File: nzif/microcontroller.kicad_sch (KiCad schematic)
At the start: 25 parts, among them U1 MCP23017_SO

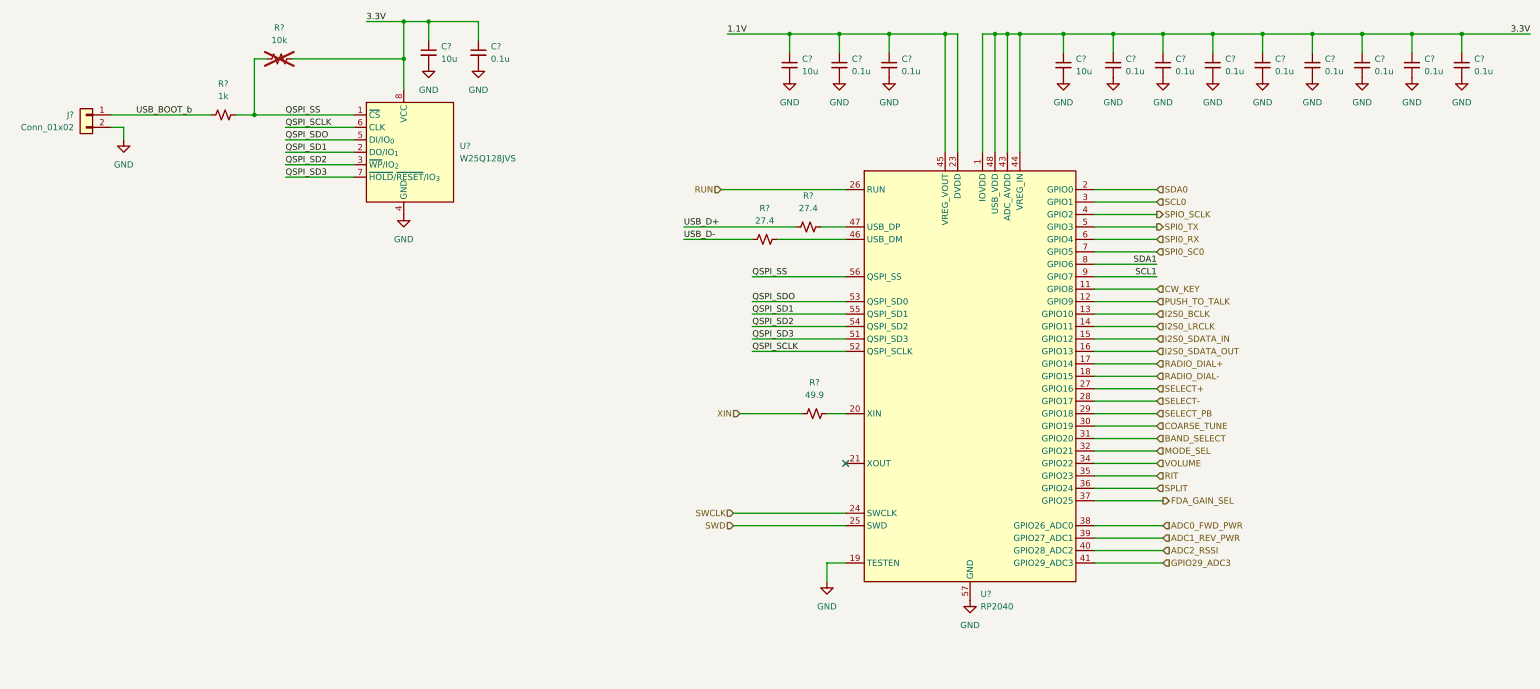
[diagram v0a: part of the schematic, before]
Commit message: Fix op amps to be correct units
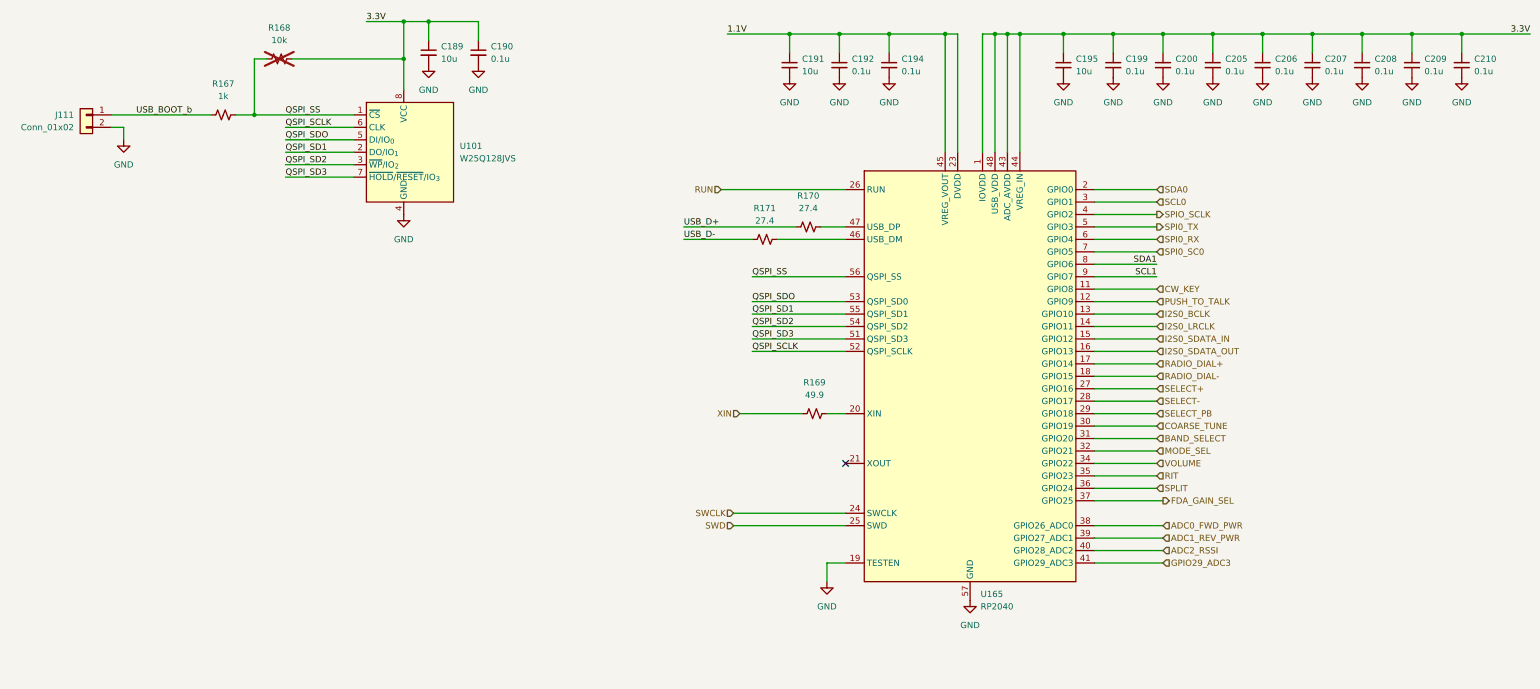
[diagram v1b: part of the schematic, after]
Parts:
- gave numbers to parts that had none: 22
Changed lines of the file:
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@@
 		(dnp no)
 		(fields_autoplaced yes)
-		(property "Reference" "C?"
+		(property "Reference" "C189"
 			(at 118.11 33.0262 0)
 			(effects
@@
 		(dnp yes)
 		(fields_autoplaced yes)
-		(property "Reference" "R?"
+		(property "Reference" "R168"
 			(at 85.09 29.21 90)
 			(effects
@@
 		(dnp no)
 		(fields_autoplaced yes)
-		(property "Reference" "R?"
+		(property "Reference" "R170"
 			(at 193.04 63.5 90)
 			(effects
@@
 		(dnp no)
 		(fields_autoplaced yes)
-		(property "Reference" "#PWR?"
+		(property "Reference" "#PWR0120"
 			(at 189.23 45.72 0)
 			(effects
@@
 		(dnp no)
 		(fields_autoplaced yes)
-		(property "Reference" "C?"
+		(property "Reference" "C194"
 			(at 212.09 35.5662 0)
 			(effects
@@
 		(dnp no)
 		(fields_autoplaced yes)
-		(property "Reference" "#PWR?"
+		(property "Reference" "#PWR0236"
 			(at 226.06 152.4 0)
 			(effects
@@
 		(dnp no)
 		(fields_autoplaced yes)
-		(property "Reference" "#PWR?"
+		(property "Reference" "#PWR0126"
 			(at 209.55 45.72 0)
 			(effects
@@
 		(dnp no)
 		(fields_autoplaced yes)
-		(property "Reference" "C?"
+		(property "Reference" "C207"
 			(at 298.45 35.5662 0)
 			(effects
@@
 		(dnp no)
 		(fields_autoplaced yes)
-		(property "Reference" "#PWR01"
+		(property "Reference" "#PWR?"
 			(at 195.58 189.23 0)
 			(effects
@@
 				)
 			)
+			(project "nzif"
+				(path "/fe42ca2f-2bb8-4d5a-9e84-807788ed632f/27cecad5-c0fc-4afc-95d0-cabdd6a56668"
+					(reference "#PWR?")
+					(unit 1)
+				)
+			)
 		)
 	)
@@
 		(dnp no)
 		(fields_autoplaced yes)
-		(property "Reference" "#PWR?"
+		(property "Reference" "#PWR0222"
 			(at 255.27 45.72 0)
 			(effects
@@
 		(dnp no)
 		(fields_autoplaced yes)
-		(property "Reference" "C?"
+		(property "Reference" "C208"
 			(at 308.61 35.5662 0)
 			(effects
@@
 		(dnp no)
 		(fields_autoplaced yes)
-		(property "Reference" "C?"
+		(property "Reference" "C190"
 			(at 128.27 33.0262 0)
 			(effects
@@
 		(dnp no)
 		(fields_autoplaced yes)
-		(property "Reference" "R?"
+		(property "Reference" "R169"
 			(at 194.31 101.6 90)
 			(effects
@@
 		(dnp no)
 		(fields_autoplaced yes)
-		(property "Reference" "#PWR?"
+		(property "Reference" "#PWR0223"
 			(at 265.43 45.72 0)
 			(effects
@@
 		(dnp no)
 		(fields_autoplaced yes)
-		(property "Reference" "R?"
+		(property "Reference" "R167"
 			(at 73.66 40.64 90)
 			(effects
@@
 		(dnp no)
 		(fields_autoplaced yes)
-		(property "Reference" "#PWR?"
+		(property "Reference" "#PWR0238"
 			(at 215.9 251.46 0)
 			(effects
@@
 		(dnp no)
 		(fields_autoplaced yes)
-		(property "Reference" "C?"
+		(property "Reference" "C210"
 			(at 328.93 35.5662 0)
 			(effects
@@
 		(dnp no)
 		(fields_autoplaced yes)
-		(property "Reference" "C?"
+		(property "Reference" "C200"
 			(at 267.97 35.5662 0)
 			(effects
@@
 		(dnp no)
 		(fields_autoplaced yes)
-		(property "Reference" "R?"
+		(property "Reference" "R171"
 			(at 184.15 66.04 90)
 			(effects
@@
 		(dnp no)
 		(fields_autoplaced yes)
-		(property "Reference" "#PWR?"
+		(property "Reference" "#PWR0226"
 			(at 275.59 45.72 0)
 			(effects
@@
 		(dnp no)
 		(fields_autoplaced yes)
-		(property "Reference" "C?"
+		(property "Reference" "C206"
 			(at 288.29 35.5662 0)
 			(effects
@@
 		(dnp no)
 		(fields_autoplaced yes)
-		(property "Reference" "#PWR?"
+		(property "Reference" "#PWR0235"
 			(at 326.39 45.72 0)
 			(effects
@@
 		(dnp no)
 		(fields_autoplaced yes)
-		(property "Reference" "U?"
+		(property "Reference" "U101"
 			(at 121.92 53.3399 0)
 			(effects
@@
 		(dnp no)
 		(fields_autoplaced yes)
-		(property "Reference" "J?"
+		(property "Reference" "J111"
 			(at 43.18 46.9899 0)
 			(effects
@@
 		(dnp no)
 		(fields_autoplaced yes)
-		(property "Reference" "C2"
+		(property "Reference" "C?"
 			(at 208.28 179.0762 0)
 			(effects
@@
 				)
 			)
+			(project "nzif"
+				(path "/fe42ca2f-2bb8-4d5a-9e84-807788ed632f/27cecad5-c0fc-4afc-95d0-cabdd6a56668"
+					(reference "C?")
+					(unit 1)
+				)
+			)
 		)
 	)
@@
 		(dnp no)
 		(fields_autoplaced yes)
-		(property "Reference" "C?"
+		(property "Reference" "C199"
 			(at 257.81 35.5662 0)
 			(effects
@@
 		(dnp no)
 		(fields_autoplaced yes)
-		(property "Reference" "#PWR?"
+		(property "Reference" "#PWR0106"
 			(at 53.34 58.42 0)
 			(effects
@@
 		(dnp no)
 		(fields_autoplaced yes)
-		(property "Reference" "#PWR02"
+		(property "Reference" "#PWR?"
 			(at 205.74 189.23 0)
 			(effects
@@
 				)
 			)
+			(project "nzif"
+				(path "/fe42ca2f-2bb8-4d5a-9e84-807788ed632f/27cecad5-c0fc-4afc-95d0-cabdd6a56668"
+					(reference "#PWR?")
+					(unit 1)
+				)
+			)
 		)
 	)
@@
 		(dnp no)
 		(fields_autoplaced yes)
-		(property "Reference" "#PWR?"
+		(property "Reference" "#PWR0237"
 			(at 196.85 148.59 0)
 			(effects
@@
 		(dnp no)
 		(fields_autoplaced yes)
-		(property "Reference" "#PWR?"
+		(property "Reference" "#PWR0232"
 			(at 306.07 45.72 0)
 			(effects
@@
 		(dnp no)
 		(fields_autoplaced yes)
-		(property "Reference" "C?"
+		(property "Reference" "C192"
 			(at 201.93 35.5662 0)
 			(effects
@@
 		(dnp no)
 		(fields_autoplaced yes)
-		(property "Reference" "#PWR?"
+		(property "Reference" "#PWR0227"
 			(at 285.75 45.72 0)
 			(effects
@@
 		(dnp no)
 		(fields_autoplaced yes)
-		(property "Reference" "#PWR?"
+		(property "Reference" "#PWR0110"
 			(at 115.57 43.18 0)
 			(effects
@@
 		(dnp no)
 		(fields_autoplaced yes)
-		(property "Reference" "C?"
+		(property "Reference" "C191"
 			(at 191.77 35.5662 0)
 			(effects
@@
 		(dnp no)
 		(fields_autoplaced yes)
-		(property "Reference" "C?"
+		(property "Reference" "C195"
 			(at 247.65 35.5662 0)
 			(effects
@@
 		(dnp no)
 		(fields_autoplaced yes)
-		(property "Reference" "#PWR?"
+		(property "Reference" "#PWR0113"
 			(at 125.73 43.18 0)
 			(effects
@@
 		(dnp no)
 		(fields_autoplaced yes)
-		(property "Reference" "U1"
+		(property "Reference" "U?"
 			(at 218.0433 189.23 0)
 			(effects
@@
 				)
 			)
+			(project "nzif"
+				(path "/fe42ca2f-2bb8-4d5a-9e84-807788ed632f/27cecad5-c0fc-4afc-95d0-cabdd6a56668"
+					(reference "U?")
+					(unit 1)
+				)
+			)
 		)
 	)
@@
 		(dnp no)
 		(fields_autoplaced yes)
-		(property "Reference" "#PWR?"
+		(property "Reference" "#PWR0129"
 			(at 245.11 45.72 0)
 			(effects
@@
 		(dnp no)
 		(fields_autoplaced yes)
-		(property "Reference" "U?"
+		(property "Reference" "U165"
 			(at 228.2033 144.78 0)
 			(effects
@@
 		(dnp no)
 		(fields_autoplaced yes)
-		(property "Reference" "#PWR?"
+		(property "Reference" "#PWR0121"
 			(at 199.39 45.72 0)
 			(effects
@@
 		(dnp no)
 		(fields_autoplaced yes)
-		(property "Reference" "C?"
+		(property "Reference" "C209"
 			(at 318.77 35.5662 0)
 			(effects
@@
 		(dnp no)
 		(fields_autoplaced yes)
-		(property "Reference" "#PWR?"
+		(property "Reference" "#PWR0107"
 			(at 110.49 73.66 0)
 			(effects
@@
 		(dnp no)
 		(fields_autoplaced yes)
-		(property "Reference" "#PWR?"
+		(property "Reference" "#PWR0230"
 			(at 295.91 45.72 0)
 			(effects
@@
 		(dnp no)
 		(fields_autoplaced yes)
-		(property "Reference" "C?"
+		(property "Reference" "C205"
 			(at 278.13 35.5662 0)
 			(effects
@@
 		(dnp no)
 		(fields_autoplaced yes)
-		(property "Reference" "C1"
+		(property "Reference" "C?"
 			(at 198.12 179.0762 0)
 			(effects
@@
 				)
 			)
+			(project "nzif"
+				(path "/fe42ca2f-2bb8-4d5a-9e84-807788ed632f/27cecad5-c0fc-4afc-95d0-cabdd6a56668"
+					(reference "C?")
+					(unit 1)
+				)
+			)
 		)
 	)
@@
 		(dnp no)
 		(fields_autoplaced yes)
-		(property "Reference" "#PWR03"
+		(property "Reference" "#PWR?"
 			(at 194.31 251.46 0)
 			(effects
@@
 				)
 			)
+			(project "nzif"
+				(path "/fe42ca2f-2bb8-4d5a-9e84-807788ed632f/27cecad5-c0fc-4afc-95d0-cabdd6a56668"
+					(reference "#PWR?")
+					(unit 1)
+				)
+			)
 		)
 	)
@@
 		(dnp no)
 		(fields_autoplaced yes)
-		(property "Reference" "#PWR?"
+		(property "Reference" "#PWR0234"
 			(at 316.23 45.72 0)
 			(effects

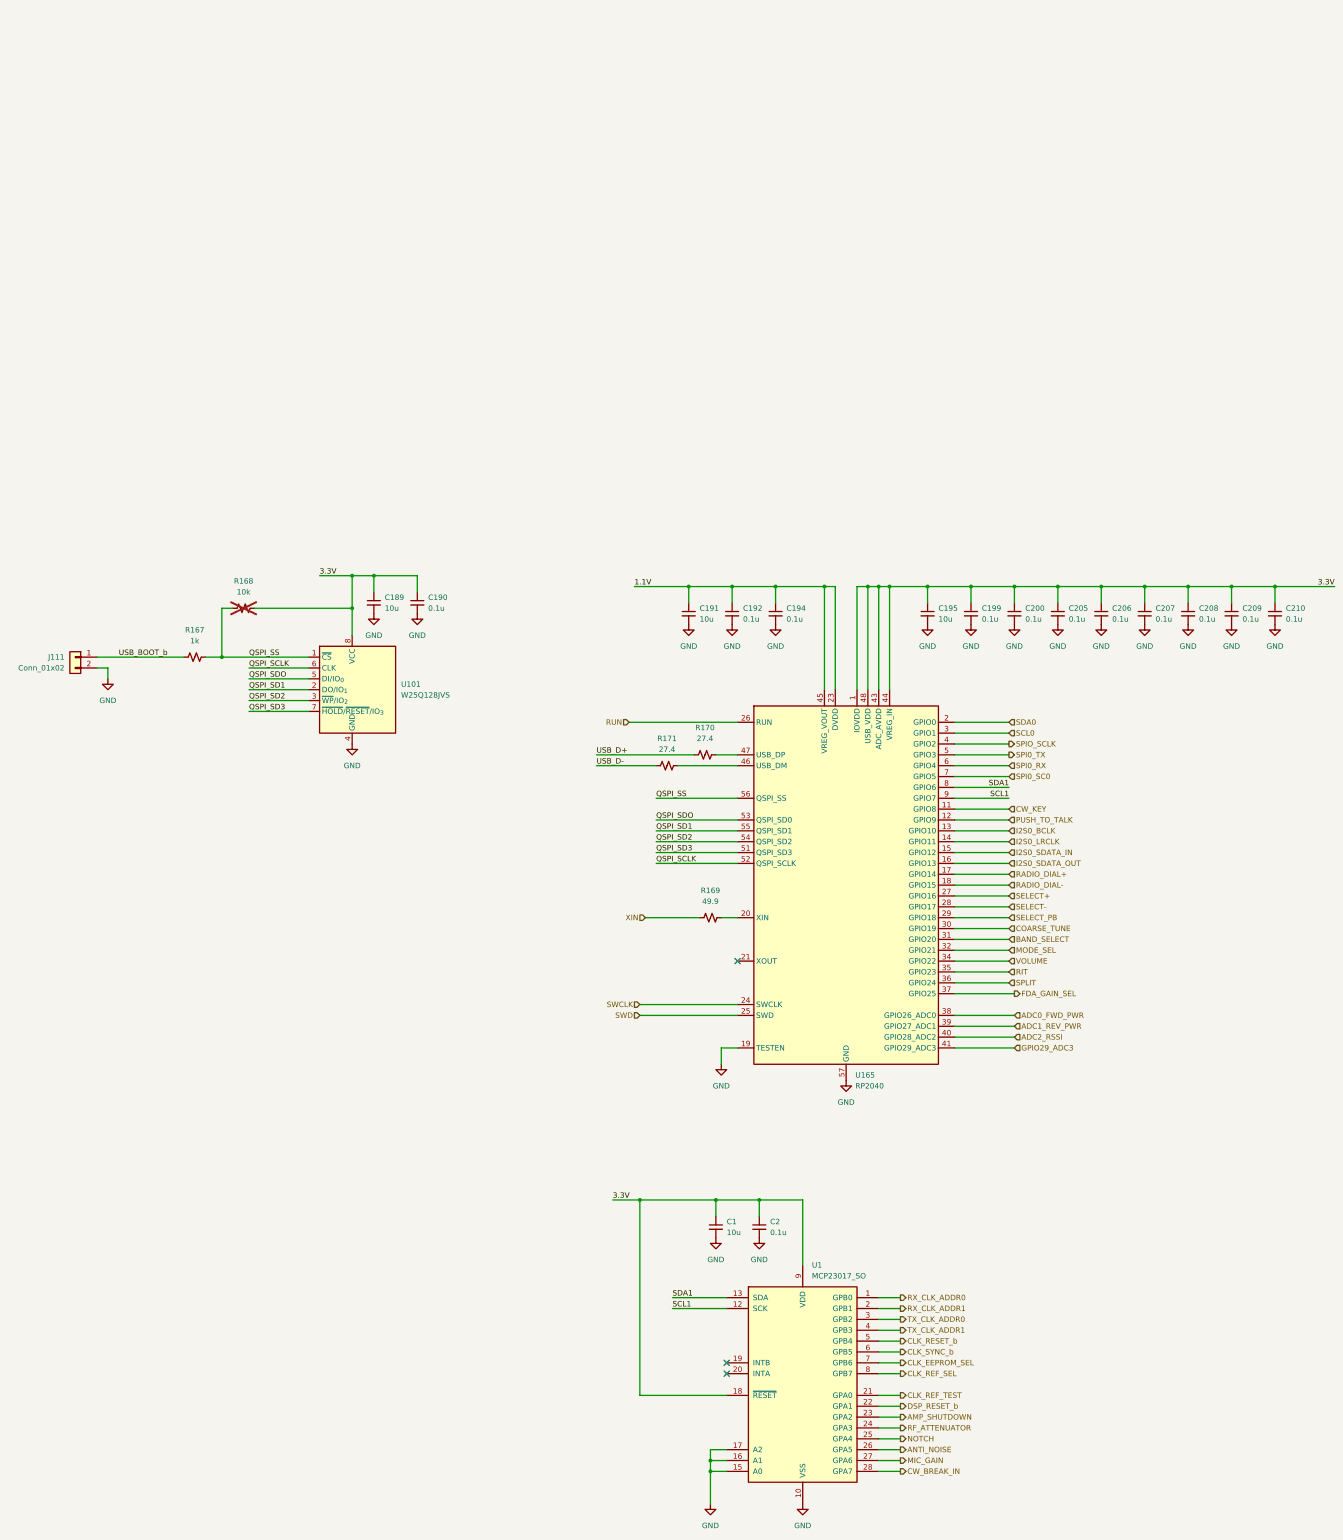
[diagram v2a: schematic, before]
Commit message: add annotations - first run of erc
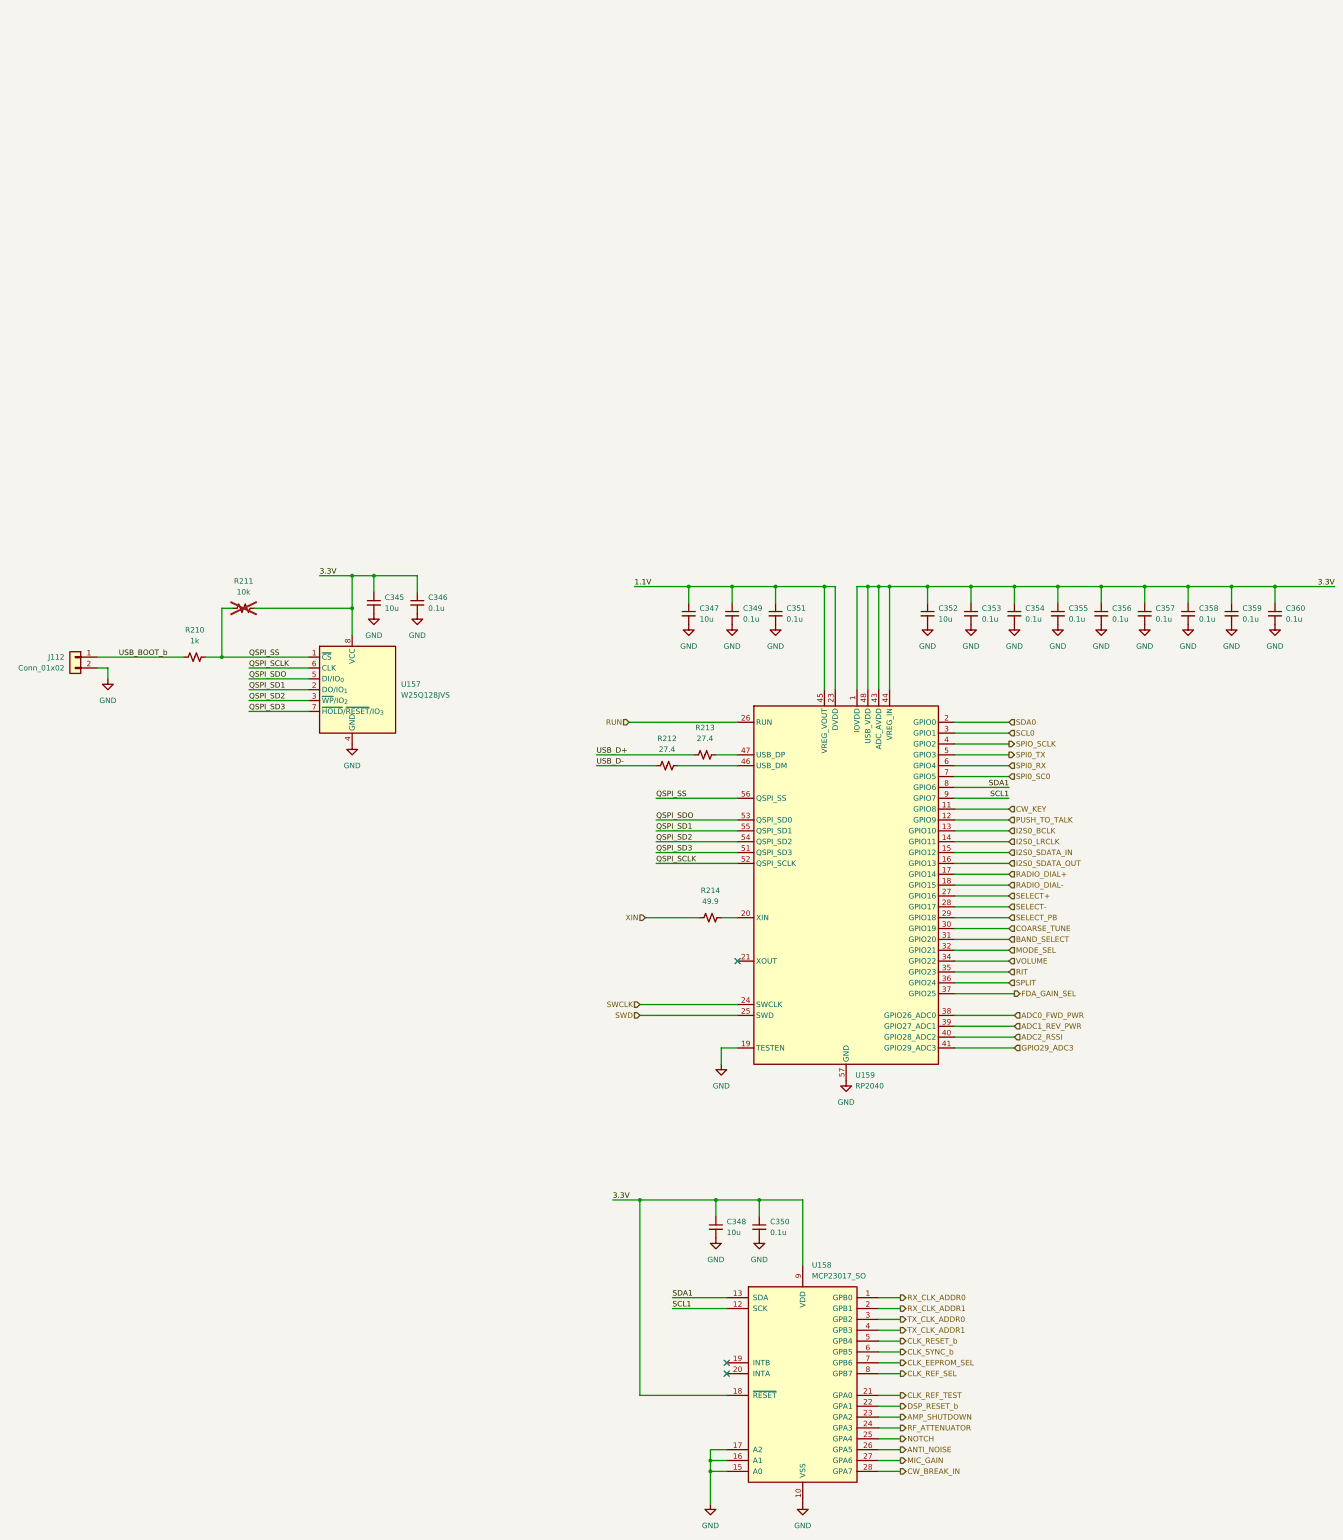
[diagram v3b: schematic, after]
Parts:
- renumbered C189 to C345, C190 to C346, C191 to C347, C1 to C348, C192 to C349, C2 to C350, C194 to C351, C195 to C352, C199 to C353, C200 to C354, C205 to C355, C206 to C356, C207 to C357, C208 to C358, C209 to C359, C210 to C360, J111 to J112, R167 to R210, R168 to R211, R171 to R212, R170 to R213, R169 to R214, U101 to U157, U1 to U158, U165 to U159
